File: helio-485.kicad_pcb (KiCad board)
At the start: 2 copper layers, 140 x 178 mm, 67 parts, among them J1 PV, J2 12V, J3 Modbus, J4 USB-C, Q1 AO3401A, Q2 AOD510, Q3 AOD510, U1 ESP32-C5-WROOM-1-N8, U2 TP5100, U3 TPS562208, U4 TPS61088, U5 S-8252, U6 THVD1400, U7 USBLC6-2, U8 TL431A, U9 TL431A

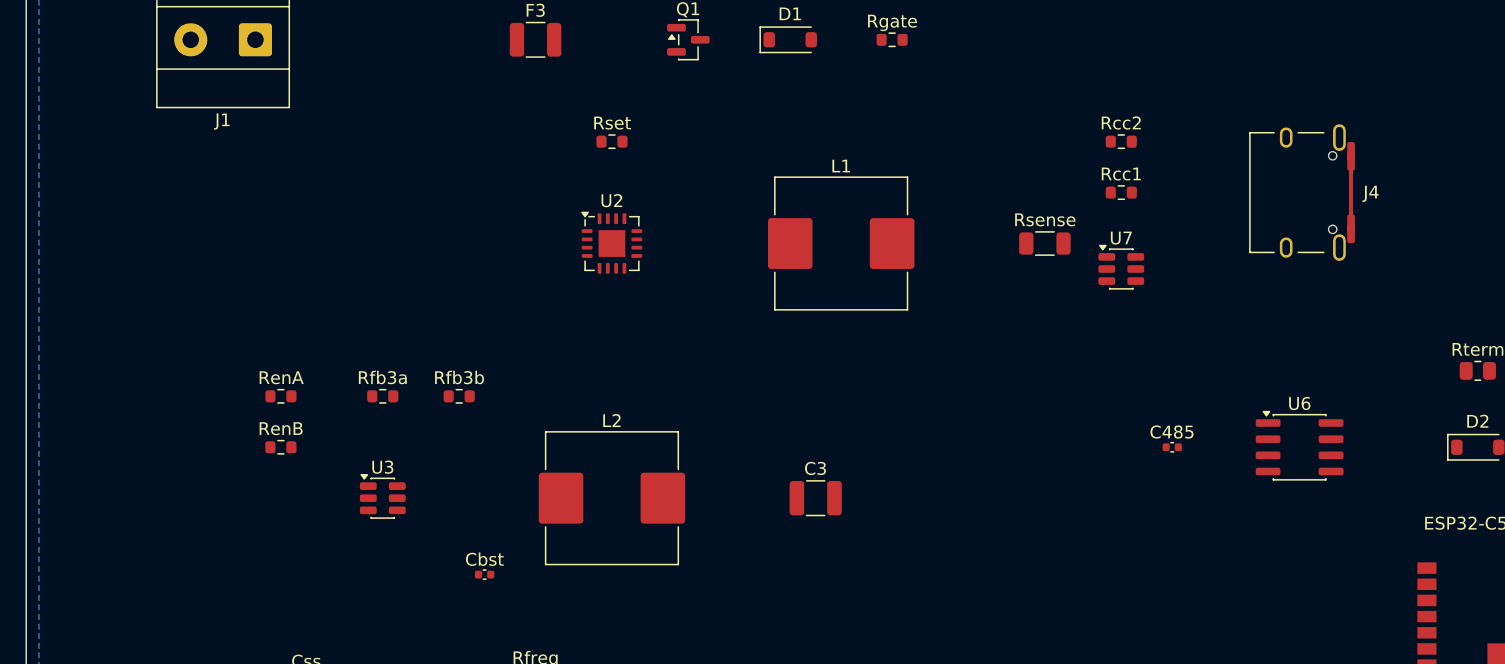
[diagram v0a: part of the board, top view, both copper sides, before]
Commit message: Put USB-C on the left edge for programming
J4 faces off the board. D+ and D- reach ESP32-C5 pins 14 and 13 through 22 ohm resistors. D3 ORs VBUS onto the 3.3 V buck so the laptop can flash the module with the pack out.
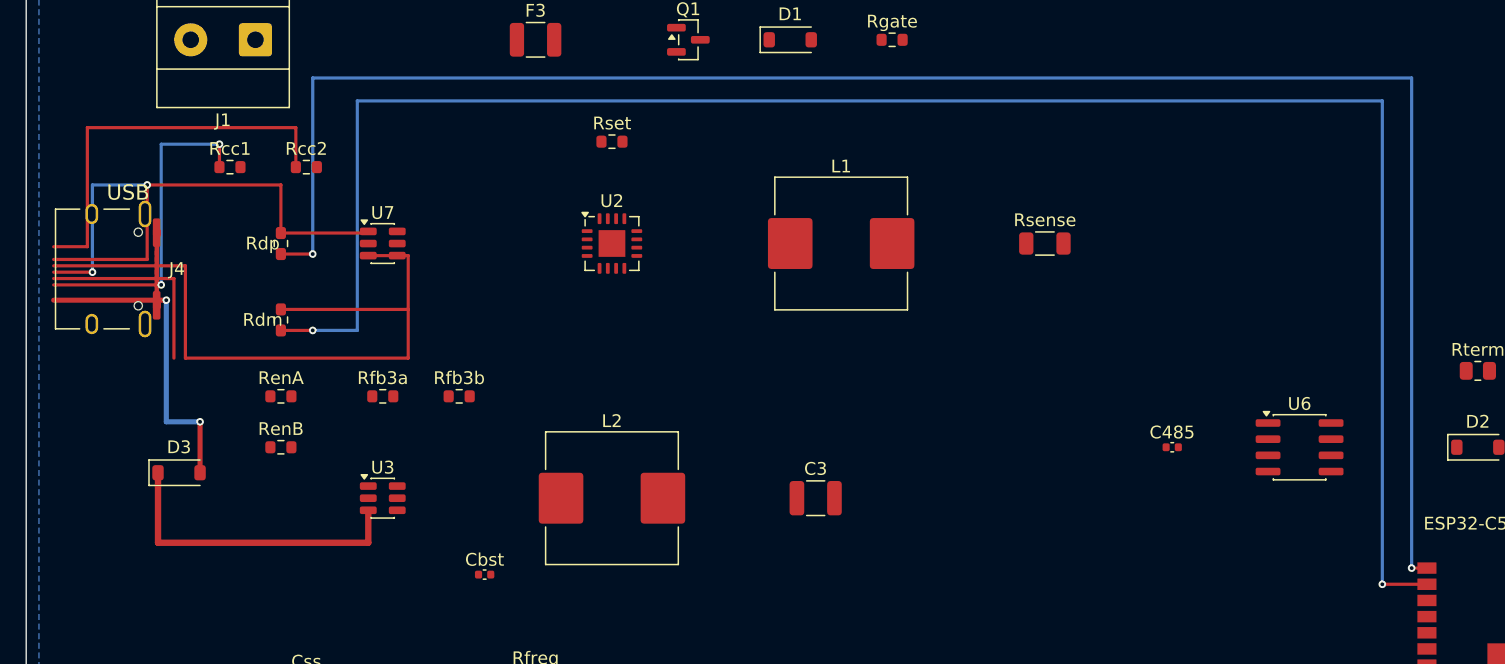
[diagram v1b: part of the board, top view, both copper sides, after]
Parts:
- added D3: B5819W, D_SOD-123, F.Cu at (12.0, 130.0)
- added Rdm: 22, R_0603_1608Metric, F.Cu at (20.0, 118.0)
- added Rdp: 22, R_0603_1608Metric, F.Cu at (20.0, 112.0)
- moved J4 94.0 mm to (6.20, 114.0)
- moved Rcc1 70.0 mm to (16.0, 106.0)
- moved Rcc2 64.0 mm to (22.0, 106.0)
- moved U7 58.0 mm to (28.0, 112.0)
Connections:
- J4 pad A6: USB_DP -> USB_DP_C
- J4 pad A7: USB_DM -> USB_DM_C
- J4 pad B6: USB_DP -> USB_DP_C
- J4 pad B7: USB_DM -> USB_DM_C
- U7 pad 1: USB_DP -> USB_DP_C
- U7 pad 3: USB_DM -> USB_DM_C
- U7 pad 4: USB_DM -> USB_DM_C
- U7 pad 6: USB_DP -> USB_DP_C
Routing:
- net USB_DM: track 0.00 -> 146.0 mm, vias 0 -> 2
- net USB_DP: track 0.00 -> 142.3 mm, vias 0 -> 2
- net USB_DM_C: track 0.00 -> 72.0 mm
- net USB_DP_C: track 0.00 -> 48.7 mm, vias 0 -> 2
- net CC2: track 0.00 -> 31.5 mm
- net CC1: track 0.00 -> 25.9 mm, vias 0 -> 2
- net USB_VBUS: track 0.00 -> 25.0 mm, vias 0 -> 2
- net VSYS: track 0.00 -> 24.6 mm
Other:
- board text added: "USB"

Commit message: Size the pack for a GloTech GEM2 on 3500 mAh cells
Six 18650s in 2S3P. The meter is 80-90 mA at 12 V, so this is about two days. J2 is yellow/purple and J3 is the meter's RS-485 pair.
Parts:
- added BT3: 18650, BatteryHolder_Keystone_1042_1x18650, F.Cu at (70.0, 18.0)
- added BT4: 18650, BatteryHolder_Keystone_1042_1x18650, F.Cu at (70.0, 45.0)
- added BT5: 18650, BatteryHolder_Keystone_1042_1x18650, F.Cu at (70.0, 72.0)
- added BT6: 18650, BatteryHolder_Keystone_1042_1x18650, F.Cu at (70.0, 99.0)
- BT1: value 18650-lower -> 18650
- BT2: value 18650-upper -> 18650
- moved BT1 108.0 mm to (70.0, 126.0)
- moved BT2 108.0 mm to (70.0, 153.0)
- moved C12A 108.0 mm to (68.0, 258.0)
- moved C12B 108.0 mm to (74.0, 258.0)
- moved C12C 108.0 mm to (80.0, 258.0)
- moved C3 108.0 mm to (62.0, 240.0)
- moved C485 108.0 mm to (90.0, 236.0)
- moved Cboot 108.0 mm to (36.0, 274.0)
- moved Cbst 108.0 mm to (36.0, 246.0)
- moved Cen 108.0 mm to (100.0, 268.0)
- moved Cmod 108.0 mm to (100.0, 272.0)
- moved Css 108.0 mm to (22.0, 254.0)
- moved Cvcc 108.0 mm to (16.0, 274.0)
- moved D1 108.0 mm to (60.0, 204.0)
- moved D2 108.0 mm to (114.0, 236.0)
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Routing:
- net PACK+: track 24.4 -> 175.4 mm, vias 0 -> 3
- net PACK-: track 16.3 -> 149.3 mm
- net MID: track 27.0 -> 135.0 mm
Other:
- board size 140 x 178 mm -> 140 x 286 mm
- board text added: "140 x 286 mm 2S3P 2-layer 2 oz"
- board text added: "2S3P"
- board text removed: "140 x 178 mm 2-layer 2 oz 1.6 mm"
- board text removed: "BT1 -"
- board text removed: "BT2 +"

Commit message: Cap the pack at two 3500 mAh cells
Three 3500 mAh cells cannot run a GEM2 for 48 hours, and the charger and protector are 2-cell parts. Board is back to 140 x 178 mm.
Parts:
- removed BT3, BT4, BT5, BT6: 18650, BatteryHolder_Keystone_1042_1x18650
- BT1, BT2: value 18650 -> 3500mAh
- moved BT1 108.0 mm to (70.0, 18.0)
- moved BT2 108.0 mm to (70.0, 45.0)
- moved C12A 108.0 mm to (68.0, 150.0)
- moved C12B 108.0 mm to (74.0, 150.0)
- moved C12C 108.0 mm to (80.0, 150.0)
- moved C3 108.0 mm to (62.0, 132.0)
- moved C485 108.0 mm to (90.0, 128.0)
- moved Cboot 108.0 mm to (36.0, 166.0)
- moved Cbst 108.0 mm to (36.0, 138.0)
- moved Cen 108.0 mm to (100.0, 160.0)
- moved Cmod 108.0 mm to (100.0, 164.0)
- moved Css 108.0 mm to (22.0, 146.0)
- moved Cvcc 108.0 mm to (16.0, 166.0)
- moved D1 108.0 mm to (60.0, 96.0)
- moved D2 108.0 mm to (114.0, 128.0)
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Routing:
- net PACK+: track 175.4 -> 24.4 mm, vias 3 -> 0
- net PACK-: track 149.3 -> 16.3 mm
- net MID: track 135.0 -> 27.0 mm
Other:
- board size 140 x 286 mm -> 140 x 178 mm
- board text added: "140 x 178 mm 2x3500 mAh 2-layer"
- board text added: "BT1 -"
- board text added: "BT2 +"
- board text removed: "140 x 286 mm 2S3P 2-layer 2 oz"
- board text removed: "2S3P"

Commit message: Replace the 18650 holders with a 2S pouch connector
Two 10 Ah flat cells cover about 43 hours at 90 mA. J5 is the pack and J6 is the balance lead.
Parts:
- removed BT1, BT2: 3500mAh, BatteryHolder_Keystone_1042_1x18650
- added J5: PACK, TerminalBlock_Phoenix_MKDS-1,5-2-5.08_1x02_P5.08mm_Horizontal, F.Cu at (78.0, 28.0)
- added J6: BAL, TerminalBlock_Phoenix_MKDS-1,5-3-5.08_1x03_P5.08mm_Horizontal, F.Cu at (78.0, 50.0)
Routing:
- net PACK-: track 16.3 -> 64.6 mm
- net PACK+: track 24.4 -> 59.9 mm
- net MID: track 27.0 -> 48.8 mm
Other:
- board text added: "140 x 178 mm 2S 10 Ah pouch"
- board text added: "BAL"
- board text added: "PACK"
- board text removed: "140 x 178 mm 2x3500 mAh 2-layer"
- board text removed: "BT1 -"
- board text removed: "BT2 +"

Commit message: Add a pack LVD and size the solar input for 2 A
The TP5100 cannot fill 10 Ah in 4 hours. Charge current is now its 2 A limit, and the boost is forced off below 6.4 V.
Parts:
- added Rens: 10k, R_0603_1608Metric, F.Cu at (108.0, 86.0)
- added Rha: 470k, R_0603_1608Metric, F.Cu at (98.0, 96.0)
- added Rpu: 100k, R_0603_1608Metric, F.Cu at (116.0, 96.0)
- added Rra: 17.4k, R_0603_1608Metric, F.Cu at (104.0, 96.0)
- added Rrb: 10.0k, R_0603_1608Metric, F.Cu at (110.0, 96.0)
- added Rsa: 43.2k, R_0603_1608Metric, F.Cu at (86.0, 96.0)
- added Rsb: 10.0k, R_0603_1608Metric, F.Cu at (92.0, 96.0)
- added U10: LM393, SOIC-8_3.9x4.9mm_P1.27mm, F.Cu at (96.0, 86.0)
- Rsense: value 0.10 -> 0.050
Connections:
- U1 pad 21: EN12 -> EN12_MCU
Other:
- board text added: "LVD 6.4V"
- board text removed: "BAL"

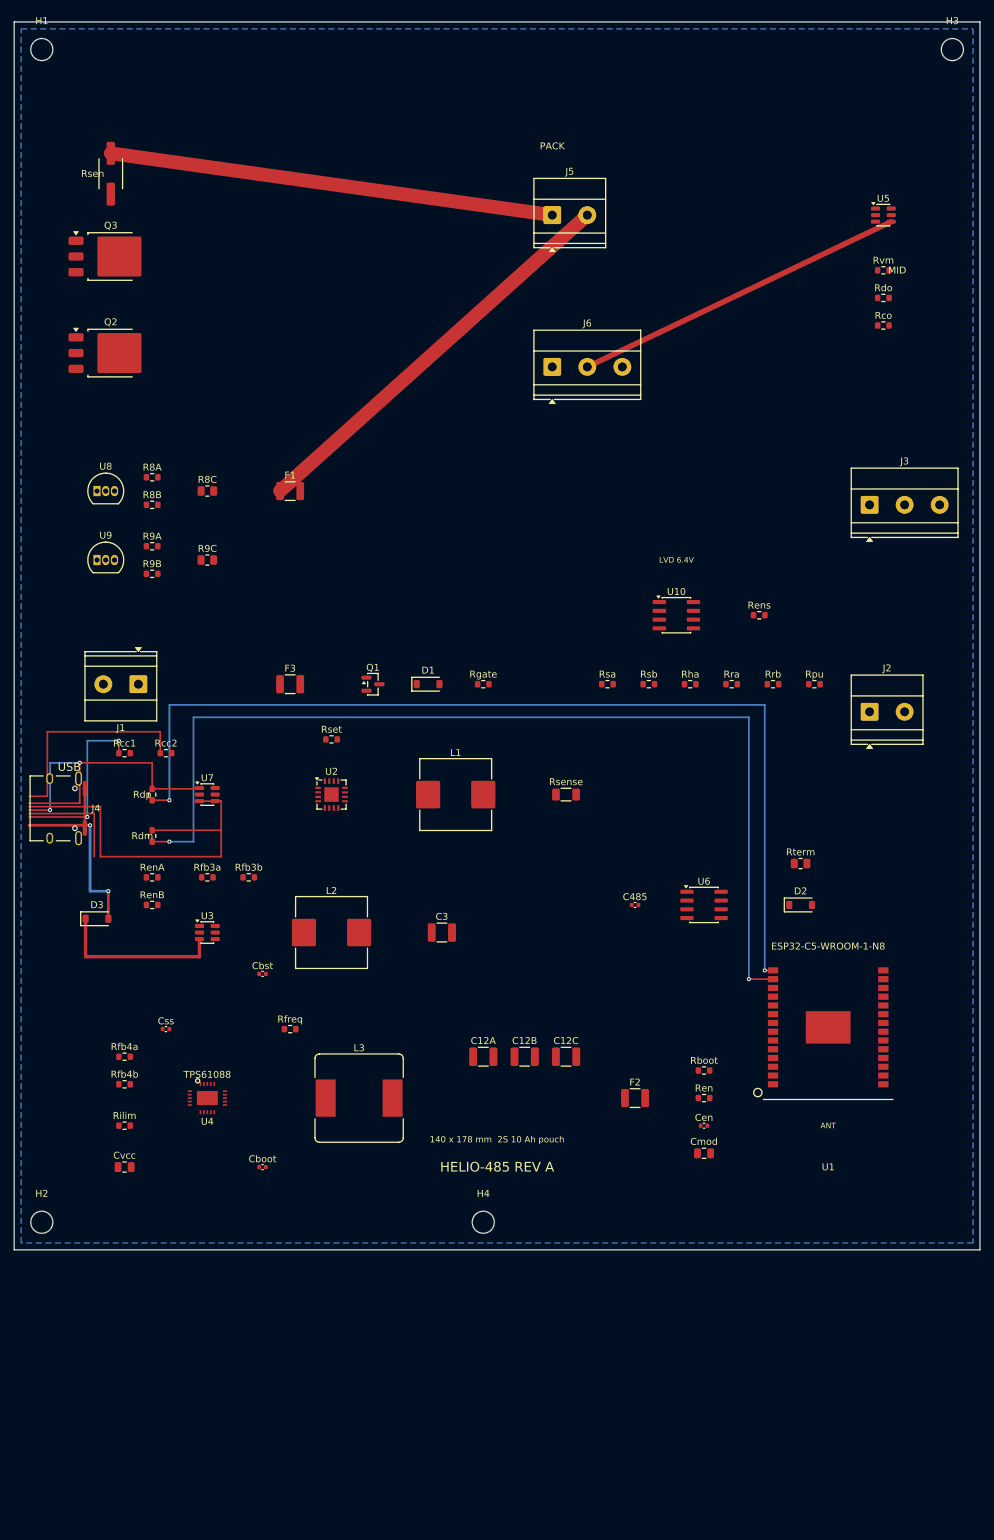
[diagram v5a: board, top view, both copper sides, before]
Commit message: Add W5500 Ethernet on the bottom edge
The ESP32-C5 has no MAC, so the jack is a W5500 on SPI. GPIO0 turns the PHY rail off when the pack has to last.
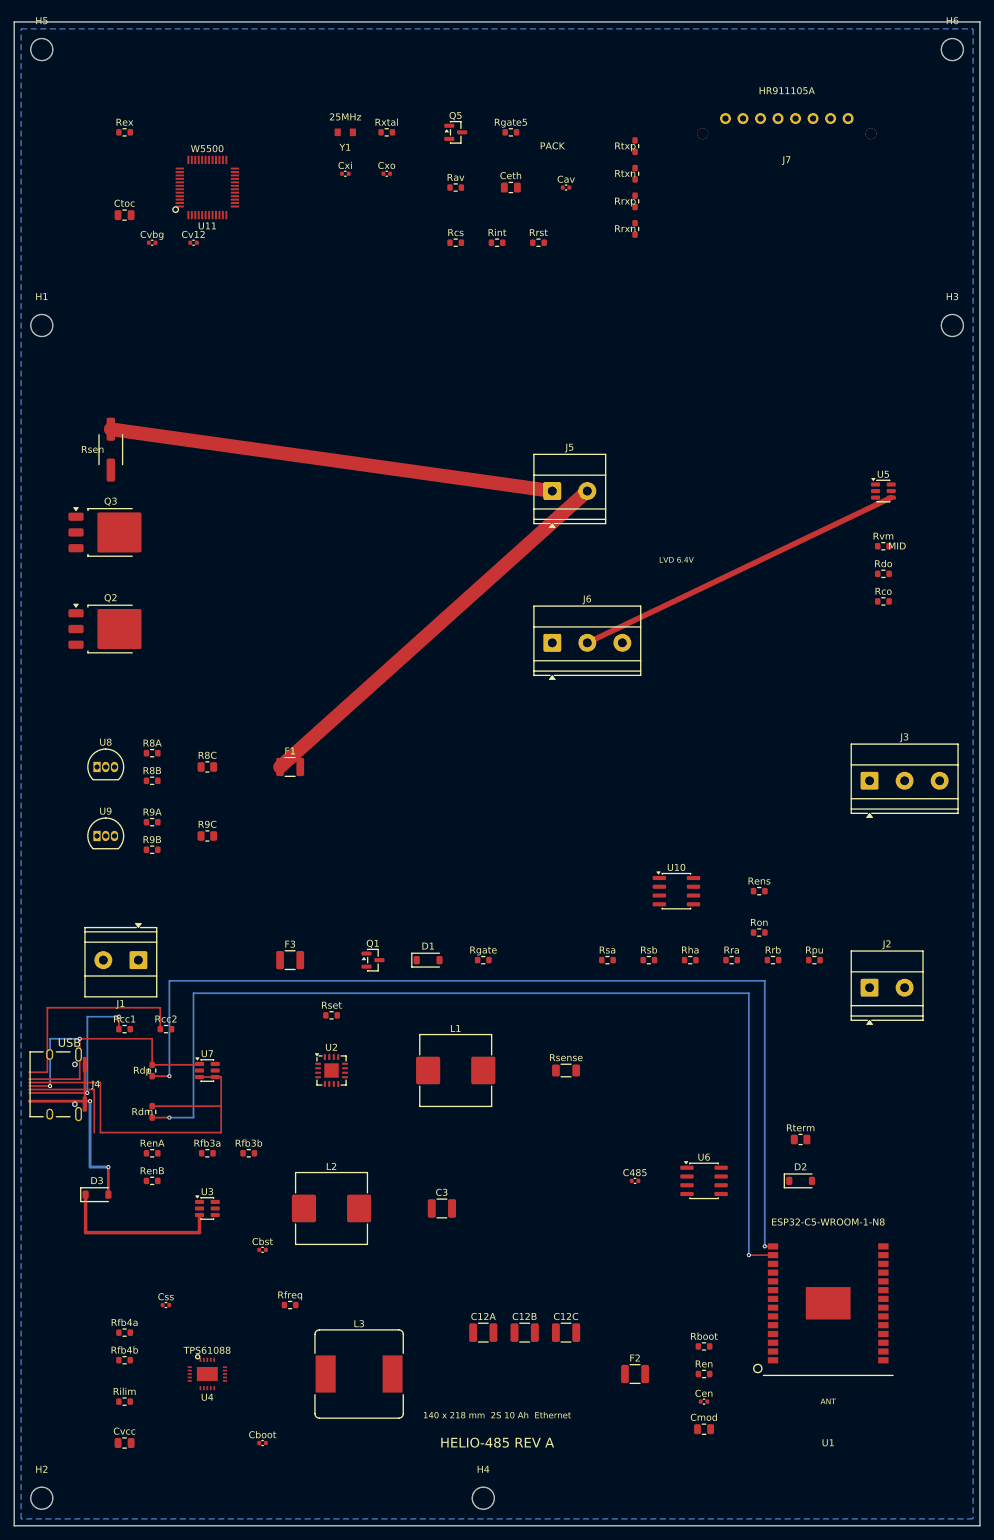
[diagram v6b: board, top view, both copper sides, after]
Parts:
- added Cav: 100n, C_0402_1005Metric, F.Cu at (80.0, 24.0)
- added Ceth: 10uF, C_0805_2012Metric, F.Cu at (72.0, 24.0)
- added Ctoc: 4.7u, C_0805_2012Metric, F.Cu at (16.0, 28.0)
- added Cv12: 10n, C_0402_1005Metric, F.Cu at (26.0, 32.0)
- added Cvbg: 10n, C_0402_1005Metric, F.Cu at (20.0, 32.0)
- added Cxi: 18p, C_0402_1005Metric, F.Cu at (48.0, 22.0)
- added Cxo: 18p, C_0402_1005Metric, F.Cu at (54.0, 22.0)
- added H5: M3, MountingHole_3.2mm_M3, F.Cu at (4.00, 4.00)
- added H6: M3, MountingHole_3.2mm_M3, F.Cu at (136.0, 4.00)
- added J7: HR911105A, Helio:RJ45-Magjack, F.Cu at (112.0, 14.0)
- added Q5: AO3401A, SOT-23, F.Cu at (64.0, 16.0)
- added Rav: 3.3, R_0603_1608Metric, F.Cu at (64.0, 24.0)
- added Rcs: 4.7k, R_0603_1608Metric, F.Cu at (64.0, 32.0)
- added Rex: 12.4k, R_0603_1608Metric, F.Cu at (16.0, 16.0)
- added Rgate5: 100k, R_0603_1608Metric, F.Cu at (72.0, 16.0)
- added Rint: 4.7k, R_0603_1608Metric, F.Cu at (70.0, 32.0)
- added Ron: 1k, R_0603_1608Metric, F.Cu at (108.0, 132.0)
- added Rrst: 4.7k, R_0603_1608Metric, F.Cu at (76.0, 32.0)
- added Rrxn: 49.9, R_0603_1608Metric, F.Cu at (90.0, 30.0)
- added Rrxp: 49.9, R_0603_1608Metric, F.Cu at (90.0, 26.0)
- added Rtxn: 49.9, R_0603_1608Metric, F.Cu at (90.0, 22.0)
- added Rtxp: 49.9, R_0603_1608Metric, F.Cu at (90.0, 18.0)
- added Rxtal: 1M, R_0603_1608Metric, F.Cu at (54.0, 16.0)
- added U11: W5500, Helio:W5500, F.Cu at (28.0, 24.0)
- added Y1: 25MHz, Helio:Crystal-3225, F.Cu at (48.0, 16.0)
- moved C12A 40.0 mm to (68.0, 190.0)
- moved C12B 40.0 mm to (74.0, 190.0)
- moved C12C 40.0 mm to (80.0, 190.0)
- moved C3 40.0 mm to (62.0, 172.0)
- moved C485 40.0 mm to (90.0, 168.0)
- moved Cboot 40.0 mm to (36.0, 206.0)
- moved Cbst 40.0 mm to (36.0, 178.0)
- moved Cen 40.0 mm to (100.0, 200.0)
- moved Cmod 40.0 mm to (100.0, 204.0)
- moved Css 40.0 mm to (22.0, 186.0)
- moved Cvcc 40.0 mm to (16.0, 206.0)
- moved D1 40.0 mm to (60.0, 136.0)
- moved D2 40.0 mm to (114.0, 168.0)
- moved D3 40.0 mm to (12.0, 170.0)
- moved F1 40.0 mm to (40.0, 108.0)
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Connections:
- U1 pad 11: (no net) -> ETH_CS
- U1 pad 12: (no net) -> ETH_MOSI
- U1 pad 23: (no net) -> ETH_INT
- U1 pad 26: (no net) -> ETH_RST
- U1 pad 4: (no net) -> ETH_SCLK
- U1 pad 5: (no net) -> ETH_MISO
- U1 pad 6: (no net) -> ETH_ON
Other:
- board size 140 x 178 mm -> 140 x 218 mm
- board text added: "140 x 218 mm 2S 10 Ah Ethernet"
- board text removed: "140 x 178 mm 2S 10 Ah pouch"

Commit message: Update the board to the KiCad 10 file format.
File version 20260206. Nets are stored by name.
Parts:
- added Ra: 10, R_0603_1608Metric, F.Cu at (109.5, 170.8)
- added Rb: 10, R_0603_1608Metric, F.Cu at (109.5, 165.2)
- added SJ1: OPEN, R_0603_1608Metric, F.Cu at (118.8, 155.6)
- D2: footprint D_SOD-123 -> SOT-23
- moved Rterm 5.13 mm to (118.8, 160.2)
- moved D2 4.80 mm to (118.8, 168.0)
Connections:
- D2 pad 1: A -> B
- D2 pad 2: B -> A
- Rterm pad 2: B -> TERM
- U6 pad 6: A -> A_DRV
- U6 pad 7: B -> B_DRV
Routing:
- net B: track 0.00 -> 9.39 mm
- net A: track 0.00 -> 9.39 mm
- net B_DRV: track 0.00 -> 8.37 mm
- net A_DRV: track 0.00 -> 8.37 mm
- net GND: track 0.00 -> 1.60 mm, vias 0 -> 1
- net RS485_DE: track 0.00 -> 1.27 mm
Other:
- board text added: "J3 A pink B green GND"
- board text added: "RS-485"
